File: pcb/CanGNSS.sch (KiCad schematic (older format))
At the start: 16 parts, among them P103 CAN, U101 MCP2515, U102 TJA1050, X101 8MHz

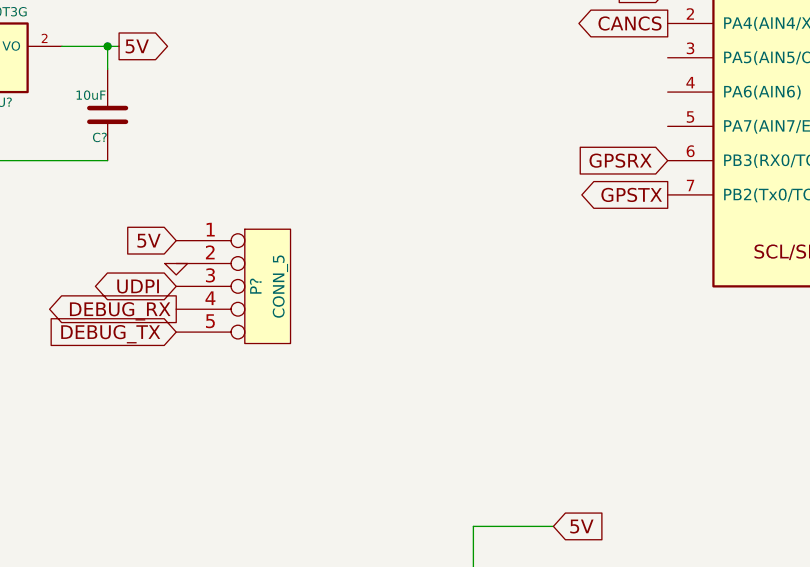
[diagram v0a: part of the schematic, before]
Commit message: Added VELNED and started NMEA2000 messages
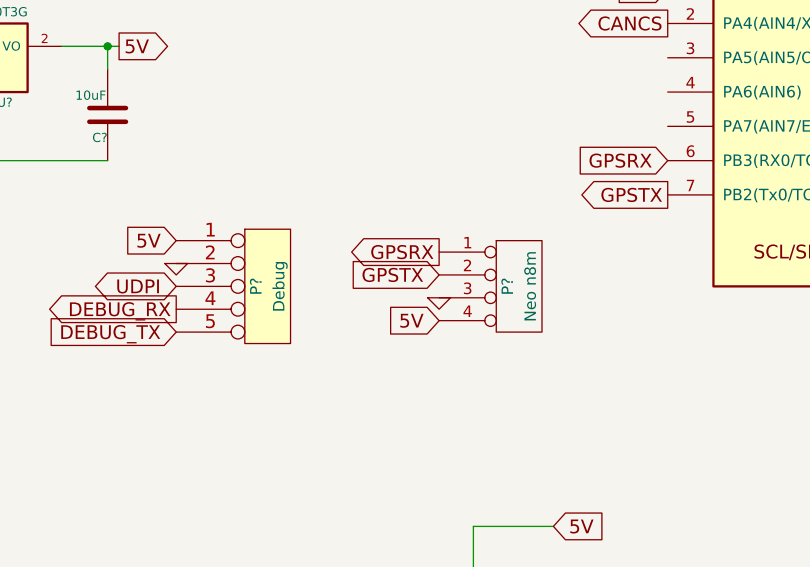
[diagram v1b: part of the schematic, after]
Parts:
- added P?: Neo n8m, symbol CONN_4
- P?: value CONN_5 -> Debug
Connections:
- net 5V: now also P?.4 (P4)
- net GND: now also P?.3 (P3)
- net GPSRX: now also P?.1 (P1)
- net GPSTX: now also P?.2 (P2)
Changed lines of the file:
@@
 P 3350 6750
 F 0 "P?" V 3300 6750 50  0000 C CNN
-F 1 "CONN_5" V 3400 6750 50  0000 C CNN
+F 1 "Debug" V 3400 6750 50  0000 C CNN
 F 2 "" H 3350 6750 60  0001 C CNN
 F 3 "" H 3350 6750 60  0001 C CNN
@@
 Text GLabel 2950 6550 0    60   Input ~ 0
 5V
+$Comp
+L CONN_4 P?
+U 1 1 648D4E0B
+P 4450 6750
+F 0 "P?" V 4400 6750 50  0000 C CNN
+F 1 "Neo n8m" V 4500 6750 50  0000 C CNN
+F 2 "" H 4450 6750 60  0001 C CNN
+F 3 "" H 4450 6750 60  0001 C CNN
+	1    4450 6750
+	1    0    0    -1
+$EndComp
+Text GLabel 4100 6600 0    60   Output ~ 0
+GPSRX
+Text GLabel 4100 6700 0    60   Input ~ 0
+GPSTX
+$Comp
+L GND #PWR?
+U 1 1 648D4F08
+P 4100 6800
+F 0 "#PWR?" H 4100 6800 30  0001 C CNN
+F 1 "GND" H 4100 6730 30  0001 C CNN
+F 2 "" H 4100 6800 60  0001 C CNN
+F 3 "" H 4100 6800 60  0001 C CNN
+	1    4100 6800
+	1    0    0    -1
+$EndComp
+Text GLabel 4100 6900 0    60   Input ~ 0
+5V
 $EndSCHEMATC

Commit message: Added ability to configure at startup
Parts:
- removed P?: Neo n8m, symbol CONN_4
- added C108: 100nF, Capacitors_SMD:C_0805, symbol C
- added U104: neo-m8n-module, Divers:neo-m8n-module, symbol neo-m8n-module
- C107: renamed from C?; value 10uF -> 100uF; footprint Capacitors_SMD:C_0805 -> Capacitors_SMD:c_elec_6.3x5.7
- P101: renamed from P?; footprint (none) -> Pin_Headers:Pin_Header_Straight_1x05
- U103: renamed from U?; footprint (none) -> TO_SOT_Packages_SMD:SOT-223-3Lead_TabPin2
- gave numbers to parts that had none: 3
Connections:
- net 5V: now also C108.2, U104.1 (Vcc)
- net GND: now also C108.1, U104.4 (Gnd)
- net GPSRX: now also U104.3 (Tx)
- net GPSTX: now also U104.2 (Rx)
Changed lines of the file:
@@
 	4050 8800 3900 8800
 $Comp
-L GND #PWR02
+L GND #PWR01
 U 1 1 61688C26
 P 5800 8650
-F 0 "#PWR02" H 5800 8650 30  0001 C CNN
+F 0 "#PWR01" H 5800 8650 30  0001 C CNN
 F 1 "GND" H 5800 8580 30  0001 C CNN
 F 2 "" H 5800 8650 60  0001 C CNN
@@
 5V
 $Comp
-L GND #PWR03
+L GND #PWR02
 U 1 1 616890A7
 P 2000 10200
-F 0 "#PWR03" H 2000 10200 30  0001 C CNN
+F 0 "#PWR02" H 2000 10200 30  0001 C CNN
 F 1 "GND" H 2000 10130 30  0001 C CNN
 F 2 "" H 2000 10200 60  0001 C CNN
@@
 $EndComp
 $Comp
-L GND #PWR04
+L GND #PWR03
 U 1 1 61689FE3
 P 600 8850
-F 0 "#PWR04" H 600 8850 30  0001 C CNN
+F 0 "#PWR03" H 600 8850 30  0001 C CNN
 F 1 "GND" H 600 8780 30  0001 C CNN
 F 2 "" H 600 8850 60  0001 C CNN
@@
 Connection ~ 1900 11000
 $Comp
-L GND #PWR05
+L GND #PWR04
 U 1 1 6168D5B4
 P 1900 11100
-F 0 "#PWR05" H 1900 11100 30  0001 C CNN
+F 0 "#PWR04" H 1900 11100 30  0001 C CNN
 F 1 "GND" H 1900 11030 30  0001 C CNN
 F 2 "" H 1900 11100 60  0001 C CNN
@@
 12v
 $Comp
-L GND #PWR06
+L GND #PWR05
 U 1 1 62C251B0
 P 1950 7000
-F 0 "#PWR06" H 1950 7000 30  0001 C CNN
+F 0 "#PWR05" H 1950 7000 30  0001 C CNN
 F 1 "GND" H 1950 6930 30  0001 C CNN
 F 2 "" H 1950 7000 60  0001 C CNN
@@
 5mA max
 $Comp
-L ATTINY3224-SS IC?
+L ATTINY3224-SS IC101
 U 1 1 648C10FB
 P 6150 6050
-F 0 "IC?" H 5400 6800 60  0000 C CNN
+F 0 "IC101" H 5400 6800 60  0000 C CNN
 F 1 "ATTINY3224-SS" H 6700 5300 60  0000 C CNN
 F 2 "SO14" H 5450 5300 60  0001 C CNN
@@
 $EndComp
 $Comp
-L NCP1117ST50T3G U?
+L NCP1117ST50T3G U103
 U 1 1 648C195D
 P 2050 5750
-F 0 "U?" H 2200 5554 40  0000 C CNN
+F 0 "U103" H 2200 5554 40  0000 C CNN
 F 1 "NCP1117ST50T3G" H 2050 5950 40  0000 C CNN
-F 2 "" H 2050 5750 60  0000 C CNN
+F 2 "TO_SOT_Packages_SMD:SOT-223-3Lead_TabPin2" H 2050 5750 60  0001 C CNN
 F 3 "" H 2050 5750 60  0000 C CNN
 	1    2050 5750
@@
 $EndComp
 $Comp
-L C C?
+L C C107
 U 1 1 648C19A8
 P 2650 6000
-F 0 "C?" H 2650 6100 40  0000 L CNN
-F 1 "10uF" H 2656 5915 40  0000 L CNN
-F 2 "Capacitors_SMD:C_0805" H 2688 5850 30  0001 C CNN
+F 0 "C107" H 2650 6100 40  0000 L CNN
+F 1 "100uF" H 2656 5915 40  0000 L CNN
+F 2 "Capacitors_SMD:c_elec_6.3x5.7" H 2688 5850 30  0001 C CNN
 F 3 "" H 2650 6000 60  0000 C CNN
 	1    2650 6000
@@
 $EndComp
 $Comp
-L C C?
+L C C106
 U 1 1 648C19F8
 P 1300 6000
-F 0 "C?" H 1300 6100 40  0000 L CNN
+F 0 "C106" H 1300 6100 40  0000 L CNN
 F 1 "10uF" H 1306 5915 40  0000 L CNN
 F 2 "Capacitors_SMD:C_0805" H 1338 5850 30  0001 C CNN
@@
 12v
 $Comp
-L GND #PWR?
+L GND #PWR06
 U 1 1 648C1BF7
 P 2050 6250
-F 0 "#PWR?" H 2050 6250 30  0001 C CNN
+F 0 "#PWR06" H 2050 6250 30  0001 C CNN
 F 1 "GND" H 2050 6180 30  0001 C CNN
 F 2 "" H 2050 6250 60  0001 C CNN
@@
 UDPI
 $Comp
-L R R?
+L R R102
 U 1 1 648C85E6
 P 7450 6050
-F 0 "R?" V 7530 6050 40  0000 C CNN
+F 0 "R102" V 7530 6050 40  0000 C CNN
 F 1 "10K" V 7457 6051 40  0000 C CNN
 F 2 "Resistors_SMD:R_0805_HandSoldering" V 7380 6050 30  0001 C CNN
@@
 DEBUG_TX
 $Comp
-L CONN_5 P?
+L CONN_5 P101
 U 1 1 648C8BBA
 P 3350 6750
-F 0 "P?" V 3300 6750 50  0000 C CNN
+F 0 "P101" V 3300 6750 50  0000 C CNN
 F 1 "Debug" V 3400 6750 50  0000 C CNN
-F 2 "" H 3350 6750 60  0001 C CNN
+F 2 "Pin_Headers:Pin_Header_Straight_1x05" H 3350 6750 60  0001 C CNN
 F 3 "" H 3350 6750 60  0001 C CNN
 	1    3350 6750
@@
 $EndComp
 $Comp
-L GND #PWR?
+L GND #PWR07
 U 1 1 648C8CF4
-P 7200 5450
-F 0 "#PWR?" H 7200 5450 30  0001 C CNN
-F 1 "GND" H 7200 5380 30  0001 C CNN
-F 2 "" H 7200 5450 60  0001 C CNN
-F 3 "" H 7200 5450 60  0001 C CNN
-	1    7200 5450
+P 7750 5550
+F 0 "#PWR07" H 7750 5550 30  0001 C CNN
+F 1 "GND" H 7750 5480 30  0001 C CNN
+F 2 "" H 7750 5550 60  0001 C CNN
+F 3 "" H 7750 5550 60  0001 C CNN
+	1    7750 5550
 	1    0    0    -1
 $EndComp
@@
 UDPI
 $Comp
-L GND #PWR?
+L GND #PWR08
 U 1 1 648C8E56
 P 2950 6650
-F 0 "#PWR?" H 2950 6650 30  0001 C CNN
+F 0 "#PWR08" H 2950 6650 30  0001 C CNN
 F 1 "GND" H 2950 6580 30  0001 C CNN
 F 2 "" H 2950 6650 60  0001 C CNN
@@
 Text GLabel 2950 6550 0    60   Input ~ 0
 5V
-$Comp
-L CONN_4 P?
-U 1 1 648D4E0B
-P 4450 6750
-F 0 "P?" V 4400 6750 50  0000 C CNN
-F 1 "Neo n8m" V 4500 6750 50  0000 C CNN
-F 2 "" H 4450 6750 60  0001 C CNN
-F 3 "" H 4450 6750 60  0001 C CNN
-	1    4450 6750
-	1    0    0    -1
-$EndComp
-Text GLabel 4100 6600 0    60   Output ~ 0
+Text GLabel 5600 7600 0    60   Output ~ 0
 GPSRX
-Text GLabel 4100 6700 0    60   Input ~ 0
+Text GLabel 5600 7450 0    60   Input ~ 0
 GPSTX
 $Comp
-L GND #PWR?
+L GND #PWR09
 U 1 1 648D4F08
-P 4100 6800
-F 0 "#PWR?" H 4100 6800 30  0001 C CNN
-F 1 "GND" H 4100 6730 30  0001 C CNN
-F 2 "" H 4100 6800 60  0001 C CNN
-F 3 "" H 4100 6800 60  0001 C CNN
-	1    4100 6800
-	1    0    0    -1
-$EndComp
-Text GLabel 4100 6900 0    60   Input ~ 0
+P 5600 7750
+F 0 "#PWR09" H 5600 7750 30  0001 C CNN
+F 1 "GND" H 5600 7680 30  0001 C CNN
+F 2 "" H 5600 7750 60  0001 C CNN
+F 3 "" H 5600 7750 60  0001 C CNN
+	1    5600 7750
+	1    0    0    -1
+$EndComp
+Text GLabel 5600 7300 0    60   Input ~ 0
+5V
+$Comp
+L neo-m8n-module U104
+U 1 1 6497F2D4
+P 6350 7350
+F 0 "U104" H 6350 7100 60  0000 C CNN
+F 1 "neo-m8n-module" H 6350 7250 60  0000 C CNN
+F 2 "Divers:neo-m8n-module" H 6250 7000 60  0001 C CNN
+F 3 "" H 6250 7000 60  0001 C CNN
+	1    6350 7350
+	1    0    0    -1
+$EndComp
+$Comp
+L C C108
+U 1 1 64980358
+P 7750 5250
+F 0 "C108" H 7750 5350 40  0000 L CNN
+F 1 "100nF" H 7756 5165 40  0000 L CNN
+F 2 "Capacitors_SMD:C_0805" H 7788 5100 30  0001 C CNN
+F 3 "" H 7750 5250 60  0000 C CNN
+	1    7750 5250
+	-1   0    0    1
+$EndComp
+Wire Wire Line
+	7200 5450 7750 5450
+Wire Wire Line
+	7750 5450 7750 5550
+Text GLabel 7750 5050 2    60   Input ~ 0
 5V
 $EndSCHEMATC
